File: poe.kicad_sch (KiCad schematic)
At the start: 34 parts, among them IC2 TPS2378DDA

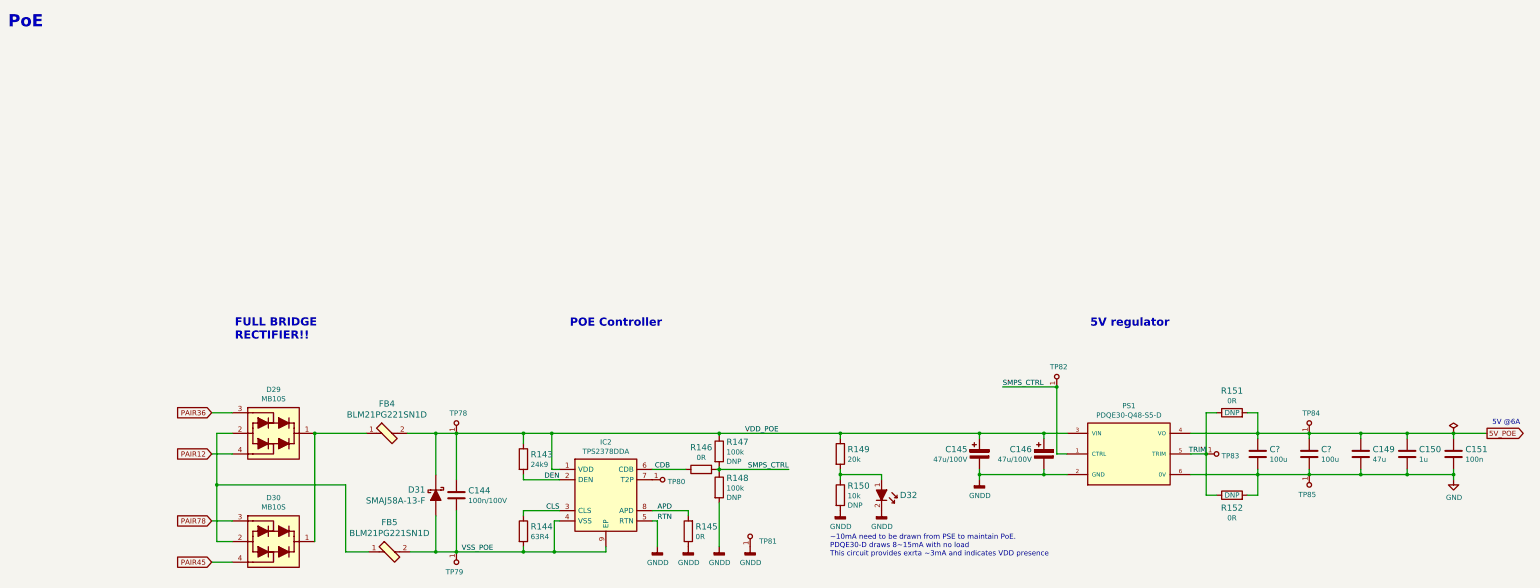
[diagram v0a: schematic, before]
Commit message: Introduce component standardization
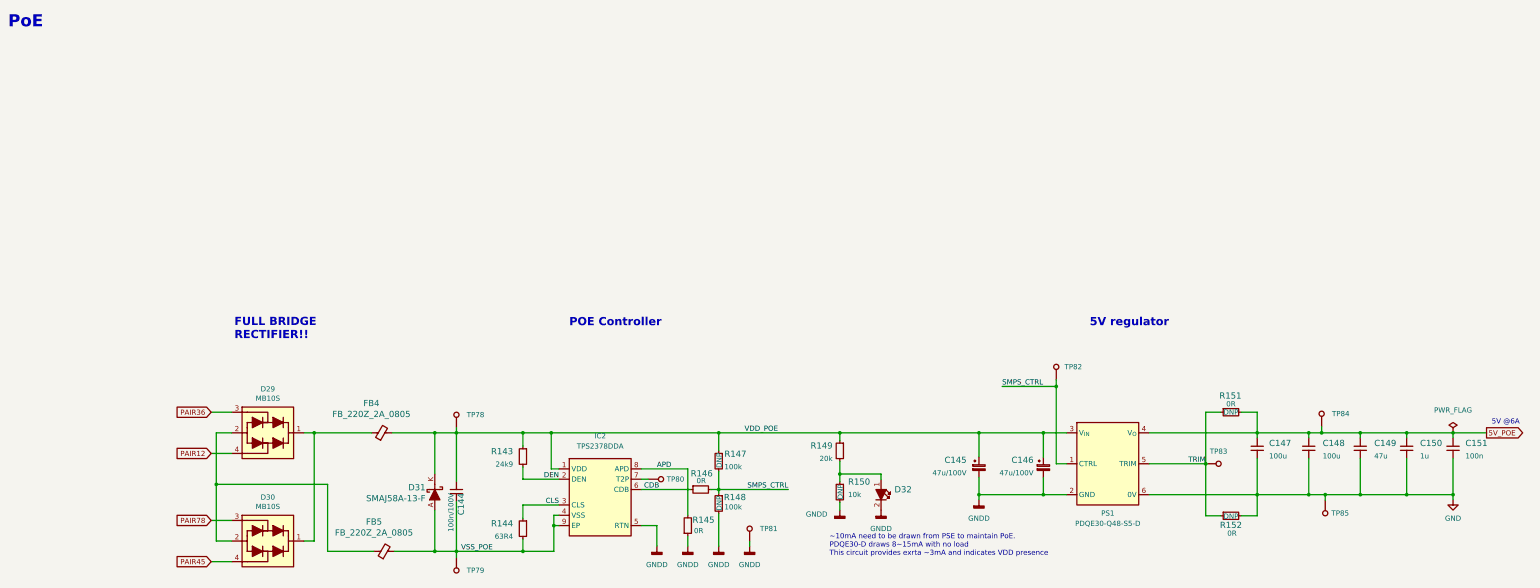
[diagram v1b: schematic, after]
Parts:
- C144: footprint sa800u-baseboard-hw-footprints:0805-cap -> sa800u-baseboard-hw-footprints:C_0805_2012Metric; Author (none) -> Antmicro; Dielectric (none) -> X7R; License (none) -> Apache-2.0; Voltage (none) -> 100V
- C145, C146: footprint sa800u-baseboard-hw-footprints:CP_Elec_10x10.5 -> sa800u-baseboard-hw-footprints:C_Elec_10x10.5mm; Author (none) -> Antmicro; License (none) -> Apache-2.0; Manufacturer PANASONIC -> Panasonic
- C147, C148: renamed from C?; value (none) -> C_100u_0805; footprint (none) -> sa800u-baseboard-hw-footprints:C_0805_2012Metric; Author (none) -> Antmicro; License (none) -> Apache-2.0; Manufacturer MURATA -> Murata
- C149: footprint sa800u-baseboard-hw-footprints:0805-cap -> sa800u-baseboard-hw-footprints:C_0805_2012Metric; Author (none) -> Antmicro; License (none) -> Apache-2.0
- C150: footprint sa800u-baseboard-hw-footprints:0402-cap -> sa800u-baseboard-hw-footprints:C_0402_1005Metric; Author (none) -> Antmicro; License (none) -> Apache-2.0
- C151: footprint sa800u-baseboard-hw-footprints:0402-cap -> sa800u-baseboard-hw-footprints:C_0402_1005Metric; Author (none) -> Antmicro; Dielectric (none) -> X5R; License (none) -> Apache-2.0; MPN 0402X104K6R3CT -> GRM155R61H104KE14D; Manufacturer Walsin -> Murata; Voltage (none) -> 50V
- D29, D30: footprint sa800u-baseboard-hw-footprints:MB10S -> sa800u-baseboard-hw-footprints:SOIC-4_4.2x5.0mm_P5.7mm; Author (none) -> Antmicro; License (none) -> Apache-2.0; Manufacturer MULTICOMP -> Multicomp
- D31: Author (none) -> Antmicro; License (none) -> Apache-2.0
- D32: footprint sa800u-baseboard-hw-footprints:LED_0603 -> sa800u-baseboard-hw-footprints:LED_0603_1608Metric_G; symbol sa800u-baseboard-hw:KP-1608EC -> sa800u-baseboard-hw:LED_G_0603_KP-1608ZGC; Author (none) -> Antmicro; License (none) -> Apache-2.0; MPN KP-1608EC -> KP-1608ZGC; Manufacturer KINGBRIGHT -> Kingbright
- FB4, FB5: value BLM21PG221SN1D -> FB_220Z_2A_0805; footprint sa800u-baseboard-hw-footprints:0805-res -> sa800u-baseboard-hw-footprints:FB_0805_2012Metric; symbol sa800u-baseboard-hw:BLM21PG221SN1D -> sa800u-baseboard-hw:FB_220Z_2A_0805; Author (none) -> Antmicro; License (none) -> Apache-2.0
- IC2: footprint sa800u-baseboard-hw-footprints:SOIC127P600X170-9N -> sa800u-baseboard-hw-footprints:SOIC-8-1EP_3.9x4.9x1.75mm_P1.27mm; Author (none) -> Antmicro; License (none) -> Apache-2.0
- PS1: footprint sa800u-baseboard-hw-footprints:PDQE30-Q48 -> sa800u-baseboard-hw-footprints:CONV_PDQE30-Q48-S5-D; Author (none) -> Antmicro; License (none) -> Apache-2.0; Manufacturer CUI -> CUI Inc
- R143: footprint sa800u-baseboard-hw-footprints:0402-res -> sa800u-baseboard-hw-footprints:R_0402_1005Metric; Author (none) -> Antmicro; License (none) -> Apache-2.0; MPN WR04X2492FTL -> CR0402-FX-2492GLF; Manufacturer WALSIN -> Bourns; Tolerance (none) -> 1%
- R144: footprint sa800u-baseboard-hw-footprints:0402-res -> sa800u-baseboard-hw-footprints:R_0402_1005Metric; Author (none) -> Antmicro; License (none) -> Apache-2.0; MPN CRCW040263R4FKED -> CR0402-FX-63R4GLF; Manufacturer Vishay -> Bourns; Tolerance (none) -> 1%
- R145, R146, R151, R152: footprint sa800u-baseboard-hw-footprints:0402-res -> sa800u-baseboard-hw-footprints:R_0402_1005Metric; Author (none) -> Antmicro; Current (none) -> 1A; License (none) -> Apache-2.0; Manufacturer PANASONIC -> Panasonic
- R147, R148: footprint sa800u-baseboard-hw-footprints:0402-res -> sa800u-baseboard-hw-footprints:R_0402_1005Metric; Author (none) -> Antmicro; License (none) -> Apache-2.0; MPN CRCW0402100KFKEDHP -> CR0402-FX-1003GLF; Manufacturer VISHAY -> Bourns; Tolerance (none) -> 1%
- R149: footprint sa800u-baseboard-hw-footprints:0603-res -> sa800u-baseboard-hw-footprints:R_0603_1608Metric; Author (none) -> Antmicro; License (none) -> Apache-2.0; MPN MCMR06X203_JTL -> CR0603-FX-2002ELF; Manufacturer MULTICOMP -> Bourns; Tolerance (none) -> 1%
- R150: footprint sa800u-baseboard-hw-footprints:0603-res -> sa800u-baseboard-hw-footprints:R_0603_1608Metric; Author (none) -> Antmicro; License (none) -> Apache-2.0; MPN CR0603-JW-103ELF -> CR0603-FX-1002ELF; Manufacturer BOURNS -> Bourns; Tolerance (none) -> 1%
- TP78, TP79, TP80, TP81, TP82, TP83, TP84, TP85: value TP -> TP_0.75mm_SMD; footprint sa800u-baseboard-hw-footprints:TP-R-1.5 -> sa800u-baseboard-hw-footprints:TP_SMD_0.75mm; symbol sa800u-baseboard-hw:TP -> sa800u-baseboard-hw:TP_0.75mm_SMD; Author (none) -> Antmicro; License (none) -> Apache-2.0
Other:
- moved on the sheet: C144, C147, C148, C149, C150, C151, D29, D30, IC2, PS1, R143, R144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

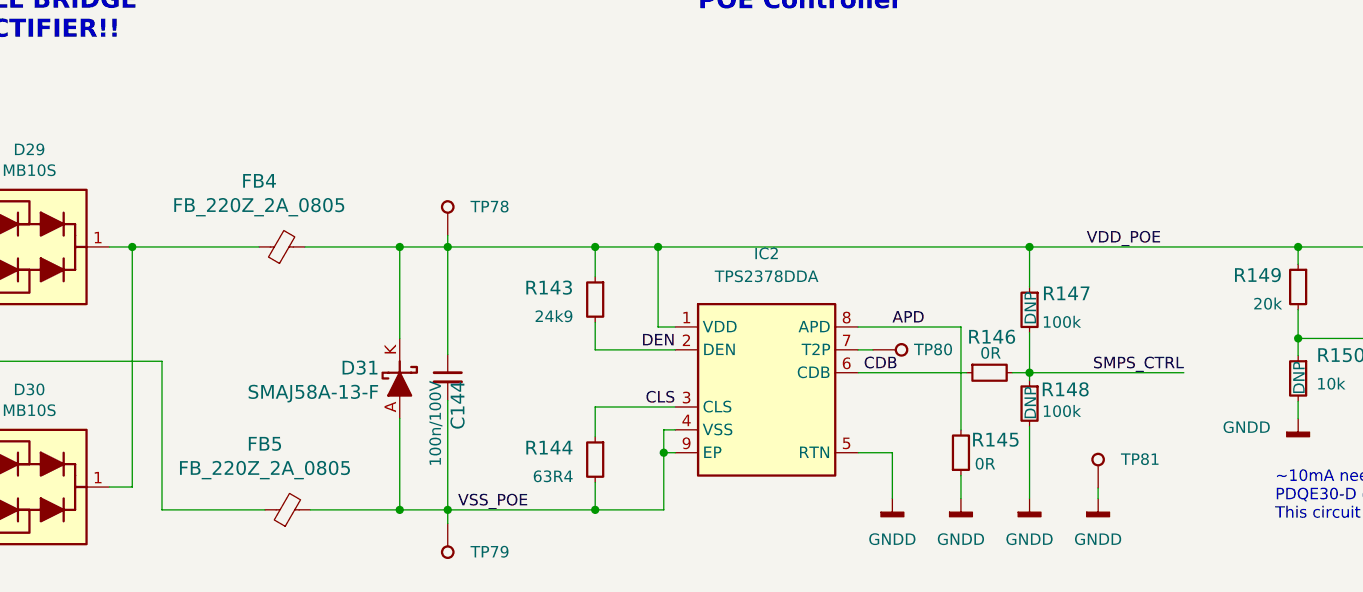
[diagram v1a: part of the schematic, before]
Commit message: Add OHP assets
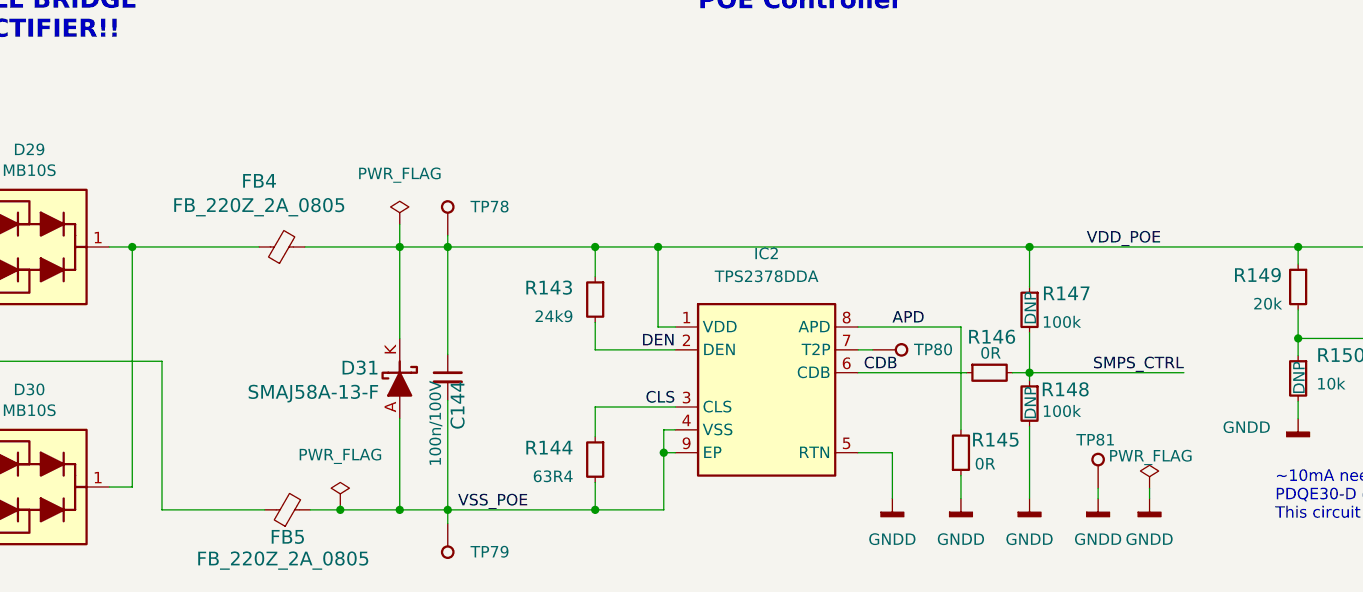
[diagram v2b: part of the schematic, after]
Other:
- company: (none) -> Antmicro Ltd.
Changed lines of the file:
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@@
   (title_block
     (title "SA800U (Snapdragon 845) Baseboard")
-    (date "2023-07-27")
-    (rev "1.0.2")
+    (date "2023-10-19")
+    (rev "1.0.3")
+    (company "Antmicro Ltd.")
     (comment 1 "www.antmicro.com")
-    (comment 2 "Antmicro Ltd.")
   )
   (junction (at 368.808 117.348) (diameter 0) (color 0 0 0 0)
@@
   (junction (at 187.833 131.318) (diameter 0) (color 0 0 0 0)
   )
+  (junction (at 111.252 146.558) (diameter 0) (color 0 0 0 0)
+  )
   (junction (at 117.856 146.558) (diameter 0) (color 0 0 0 0)
   )
@@
     (stroke (width 0) (type default) (color 0 0 0 0))
   )
+  (wire (pts (xy 201.168 144.145) (xy 201.168 145.288))
+    (stroke (width 0) (type default) (color 0 0 0 0))
+  )
   (wire (pts (xy 333.248 117.348) (xy 333.248 118.618))
     (stroke (width 0) (type default) (color 0 0 0 0))
@@
     (stroke (width 0) (type default) (color 0 0 0 0))
   )
+  (wire (pts (xy 111.252 146.05) (xy 111.252 146.558))
+    (stroke (width 0) (type default) (color 0 0 0 0))
+  )
   (wire (pts (xy 168.783 126.238) (xy 180.213 126.238))
     (stroke (width 0) (type default) (color 0 0 0 0))
@@
     (stroke (width 0) (type default) (color 0 0 0 0))
   )
-  (wire (pts (xy 107.95 146.558) (xy 117.856 146.558))
+  (wire (pts (xy 107.95 146.558) (xy 111.252 146.558))
     (stroke (width 0) (type default) (color 0 0 0 0))
   )
@@
     (stroke (width 0) (type default) (color 0 0 0 0))
   )
+  (wire (pts (xy 117.856 114.808) (xy 117.856 117.348))
+    (stroke (width 0) (type default) (color 0 0 0 0))
+  )
   (wire (pts (xy 67.818 149.098) (xy 62.738 149.098))
     (stroke (width 0) (type default) (color 0 0 0 0))
@@
     (stroke (width 0) (type default) (color 0 0 0 0))
   )
+  (wire (pts (xy 111.252 146.558) (xy 117.856 146.558))
+    (stroke (width 0) (type default) (color 0 0 0 0))
+  )
   (wire (pts (xy 357.378 118.618) (xy 357.378 117.348))
     (stroke (width 0) (type default) (color 0 0 0 0))
@@
     (pin "1")
   )
-  (symbol (lib_id "sa800u-baseboard-hw:C_47u_ELEC_100V") (at 267.843 123.317 0) (unit 1)
+  (symbol (lib_name "C_47u_ELEC_100V_1") (lib_id "sa800u-baseboard-hw:C_47u_ELEC_100V") (at 267.843 123.317 0) (unit 1)
     (in_bom yes) (on_board yes) (fields_autoplaced)
     (property "Reference" "C146" (id 0) (at 265.43 124.0536 0)
@@
   (symbol (lib_id "sa800u-baseboard-hw:FB_220Z_2A_0805") (at 102.87 146.558 0) (unit 1)
     (in_bom yes) (on_board yes)
-    (property "Reference" "FB5" (id 0) (at 102.87 139.2682 0)
+    (property "Reference" "FB5" (id 0) (at 105.41 149.606 0)
       (effects (font (size 1.524 1.524)))
     )
-    (property "Value" "FB_220Z_2A_0805" (id 1) (at 102.87 141.9606 0)
+    (property "Value" "FB_220Z_2A_0805" (id 1) (at 104.902 152.019 0)
       (effects (font (size 1.524 1.524)))
     )
@@
     (pin "2")
   )
-  (symbol (lib_id "sa800u-baseboard-hw:MB10S") (at 67.818 138.938 0) (unit 1)
+  (symbol (lib_name "MB10S_1") (lib_id "sa800u-baseboard-hw:MB10S") (at 67.818 138.938 0) (unit 1)
     (in_bom yes) (on_board yes)
     (property "Reference" "D30" (id 0) (at 76.708 133.223 0))
@@
   )
   (symbol (lib_id "sa800u-baseboard-hw:TP_0.75mm_SMD") (at 195.453 144.145 90) (unit 1)
-    (in_bom yes) (on_board yes) (fields_autoplaced)
-    (property "Reference" "TP81" (id 0) (at 197.993 140.9699 90)
+    (in_bom yes) (on_board yes)
+    (property "Reference" "TP81" (id 0) (at 193.04 138.811 90)
       (effects (font (size 1.27 1.27)) (justify right))
     )
@@
     )
     (pin "1")
+  )
+  (symbol (lib_id "sa800u-baseboard-hw:PWR_FLAG") (at 201.168 144.145 0) (unit 1)
+    (in_bom yes) (on_board yes)
+    (property "Reference" "#FLG0102" (id 0) (at 201.168 142.24 0)
+      (effects (font (size 1.27 1.27)) hide)
+    )
+    (property "Value" "PWR_FLAG" (id 1) (at 201.295 140.589 0))
+    (property "Footprint" "" (id 2) (at 201.168 144.145 0)
+      (effects (font (size 1.27 1.27)) hide)
+    )
+    (property "Datasheet" "~" (id 3) (at 201.168 144.145 0)
+      (effects (font (size 1.27 1.27)) hide)
+    )
+    (pin "1")
+  )
+  (symbol (lib_id "sa800u-baseboard-hw:PWR_FLAG") (at 111.252 146.05 0) (unit 1)
+    (in_bom yes) (on_board yes)
+    (property "Reference" "#FLG0103" (id 0) (at 111.252 144.145 0)
+      (effects (font (size 1.27 1.27)) hide)
+    )
+    (property "Value" "PWR_FLAG" (id 1) (at 111.252 140.462 0))
+    (property "Footprint" "" (id 2) (at 111.252 146.05 0)
+      (effects (font (size 1.27 1.27)) hide)
+    )
+    (property "Datasheet" "~" (id 3) (at 111.252 146.05 0)
+      (effects (font (size 1.27 1.27)) hide)
+    )
+    (pin "1")
+  )
+  (symbol (lib_id "sa800u-baseboard-hw:GNDD") (at 201.168 145.288 0) (unit 1)
+    (in_bom yes) (on_board yes) (fields_autoplaced)
+    (property "Reference" "#PWR0106" (id 0) (at 201.168 151.638 0)
+      (effects (font (size 1.27 1.27)) hide)
+    )
+    (property "Value" "GNDD" (id 1) (at 201.168 149.86 0))
+    (property "Footprint" "" (id 2) (at 201.168 145.288 0)
+      (effects (font (size 1.27 1.27)) hide)
+    )
+    (property "Datasheet" "" (id 3) (at 201.168 145.288 0)
+      (effects (font (size 1.27 1.27)) hide)
+    )
+    (property "Author" "Antmicro" (id 4) (at 216.408 152.908 0)
+      (effects (font (size 1.27 1.27) (thickness 0.15)) (justify left bottom) hide)
+    )
+    (property "License" "Apache-2.0" (id 5) (at 216.408 155.448 0)
+      (effects (font (size 1.27 1.27) (thickness 0.15)) (justify left bottom) hide)
+    )
+    (pin "1")
+  )
+  (symbol (lib_id "sa800u-baseboard-hw:PWR_FLAG") (at 117.856 114.808 0) (unit 1)
+    (in_bom yes) (on_board yes)
+    (property "Reference" "#FLG0101" (id 0) (at 117.856 112.903 0)
+      (effects (font (size 1.27 1.27)) hide)
+    )
+    (property "Value" "PWR_FLAG" (id 1) (at 117.856 109.22 0))
+    (property "Footprint" "" (id 2) (at 117.856 114.808 0)
+      (effects (font (size 1.27 1.27)) hide)
+    )
+    (property "Datasheet" "~" (id 3) (at 117.856 114.808 0)
+      (effects (font (size 1.27 1.27)) hide)
+    )
+    (pin "1")
